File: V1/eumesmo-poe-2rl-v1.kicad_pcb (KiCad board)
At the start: 4 copper layers, 82.5 x 45 mm, 105 parts, among them J1 USB_C_Receptacle_USB2.0, J2 250-202, J3 RJ45 JACK, J4 250-202, K1 G5NB-1A-E-DC5, K2 G5NB-1A-E-DC5, Q1 UMH3N, Q2 MMBT2222A, Q3 WPM2015-3/TR, Q4 LMUN2211LT1G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

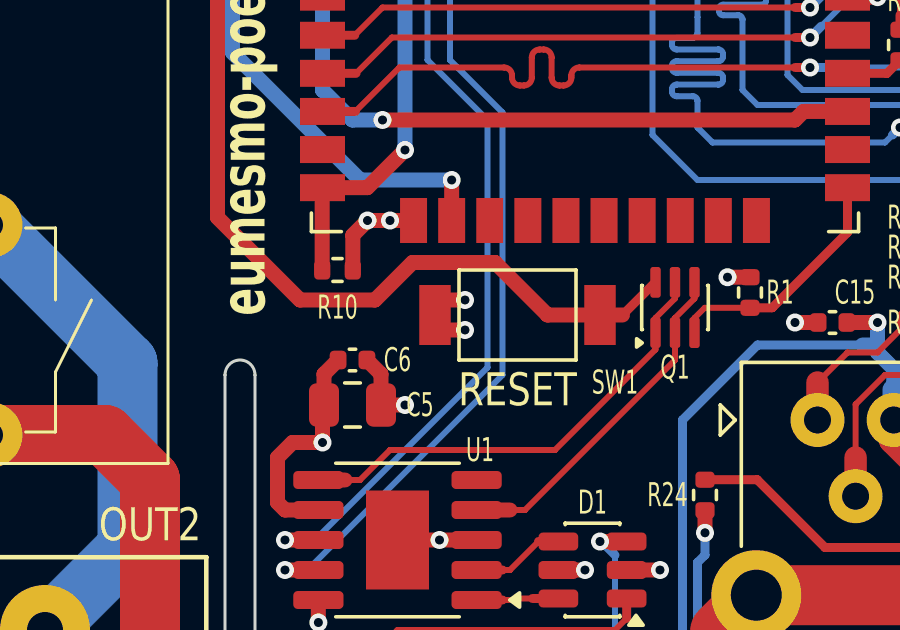
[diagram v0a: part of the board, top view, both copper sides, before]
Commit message: Rerouted TX/RX pairs between magjack and PHY.
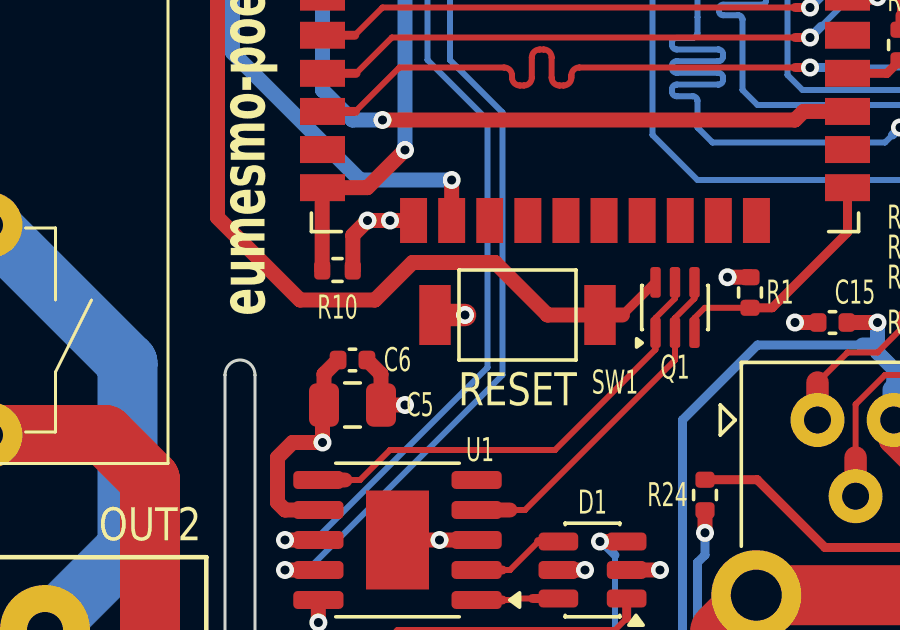
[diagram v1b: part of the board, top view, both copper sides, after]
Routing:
- net 5VUSB: track 73.8 -> 68.4 mm
- net GND: track 71.3 -> 70.3 mm, vias 51 -> 50
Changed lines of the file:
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@@
 	)
 	(segment
-		(start 99.6125 105)
+		(start 112.5 93.49)
+		(end 102.26 93.49)
+		(width 1)
+		(layer "In2.Cu")
+		(net "+3V3")
+	)
+	(segment
+		(start 99.6125 104.25)
 		(end 99.6125 101.3875)
+		(width 1)
+		(layer "In2.Cu")
+		(net "+3V3")
+	)
+	(segment
+		(start 99.6125 105)
+		(end 99.6125 104.25)
 		(width 0.5)
 		(layer "In2.Cu")
@@
 	(segment
 		(start 113.25 93.49)
-		(end 102.26 93.49)
+		(end 112.5 93.49)
 		(width 0.5)
 		(layer "In2.Cu")
@@
 		(start 99.6125 101.3875)
 		(end 99.75 101.25)
-		(width 0.5)
+		(width 1)
 		(layer "In2.Cu")
 		(net "+3V3")
@@
 		(start 99.75 101.25)
 		(end 99.75 99)
-		(width 0.5)
+		(width 1)
 		(layer "In2.Cu")
 		(net "+3V3")
@@
 	)
 	(segment
-		(start 104.5 94.25)
-		(end 103.5 94.25)
-		(width 0.5)
-		(layer "F.Cu")
-		(net "GND")
-	)
-	(segment
 		(start 102 91.6)
 		(end 101.25 91.6)
@@
 	)
 	(segment
-		(start 104.5 95.25)
-		(end 103.5 95.25)
-		(width 0.5)
+		(start 104.5 94.75)
+		(end 103.5 94.75)
+		(width 0.75)
 		(layer "F.Cu")
 		(net "GND")
@@
 	)
 	(via
-		(at 104.5 95.25)
+		(at 104.5 94.75)
 		(size 0.6)
 		(drill 0.3)
@@
 	)
 	(via
-		(at 104.5 94.25)
-		(size 0.6)
-		(drill 0.3)
-		(layers "F.Cu" "B.Cu")
-		(capping no)
-		(covering
-			(front no)
-			(back no)
-		)
-		(plugging
-			(front no)
-			(back no)
-		)
-		(filling no)
-		(net "GND")
-	)
-	(via
 		(at 156.75 110.5)
 		(size 0.6)
@@
 	)
 	(segment
+		(start 128 90.5)
+		(end 122.75 90.5)
+		(width 1)
+		(layer "In2.Cu")
+		(net "+3V3A")
+	)
+	(segment
 		(start 123.98 92.148)
 		(end 122.75 92.148)
-		(width 0.5)
+		(width 0.75)
 		(layer "In2.Cu")
 		(net "+3V3A")
@@
 	(segment
 		(start 129 89.5)
-		(end 128.25 90.25)
+		(end 128.5 90)
 		(width 0.5)
 		(layer "In2.Cu")
@@
 	)
 	(segment
-		(start 128.25 90.25)
-		(end 122.75 90.25)
-		(width 0.5)
+		(start 128.5 90)
+		(end 128 90.5)
+		(width 1)
 		(layer "In2.Cu")
 		(net "+3V3A")
@@
 	)
 	(segment
-		(start 146.25 85)
-		(end 144.25 83)
+		(start 107.75 102)
+		(end 107.75 103.25)
 		(width 1)
 		(layer "In2.Cu")
@@
 	)
 	(segment
-		(start 136 83)
-		(end 134 85)
+		(start 144.5 83.25)
+		(end 138.75 83.25)
 		(width 1)
 		(layer "In2.Cu")
@@
 	)
 	(segment
-		(start 113.25 96.5)
-		(end 107.75 102)
+		(start 134 88)
+		(end 134 88.75)
 		(width 1)
 		(layer "In2.Cu")
@@
 	)
 	(segment
-		(start 134 85)
-		(end 134 94.5)
+		(start 147.25 85)
+		(end 146.25 85)
 		(width 1)
 		(layer "In2.Cu")
@@
 	)
 	(segment
-		(start 144.25 83)
-		(end 136 83)
+		(start 113.25 96.5)
+		(end 107.75 102)
 		(width 1)
 		(layer "In2.Cu")
@@
 	)
 	(segment
-		(start 147.25 85)
-		(end 146.25 85)
+		(start 146.25 85)
+		(end 144.5 83.25)
 		(width 1)
 		(layer "In2.Cu")
@@
 	)
 	(segment
-		(start 107.75 102)
-		(end 107.75 103.25)
+		(start 106.352 107.5)
+		(end 102.6 107.5)
 		(width 1)
 		(layer "In2.Cu")
@@
 	)
 	(segment
-		(start 132 96.5)
-		(end 113.25 96.5)
+		(start 138.75 83.25)
+		(end 134 88)
 		(width 1)
 		(layer "In2.Cu")
@@
 	)
 	(segment
-		(start 106.352 107.5)
-		(end 102.6 107.5)
+		(start 126.25 96.5)
+		(end 113.25 96.5)
 		(width 1)
 		(layer "In2.Cu")
@@
 	)
 	(segment
-		(start 134 94.5)
-		(end 132 96.5)
+		(start 106.352 107.5)
+		(end 106.352 104.648)
 		(width 1)
 		(layer "In2.Cu")
@@
 	)
 	(segment
-		(start 106.352 107.5)
-		(end 106.352 104.648)
+		(start 106.352 104.648)
+		(end 107.75 103.25)
 		(width 1)
 		(layer "In2.Cu")
@@
 	)
 	(segment
-		(start 106.352 104.648)
-		(end 107.75 103.25)
+		(start 134 88.75)
+		(end 126.25 96.5)
 		(width 1)
 		(layer "In2.Cu")
